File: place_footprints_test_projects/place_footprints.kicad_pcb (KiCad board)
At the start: 2 copper layers, 65 parts

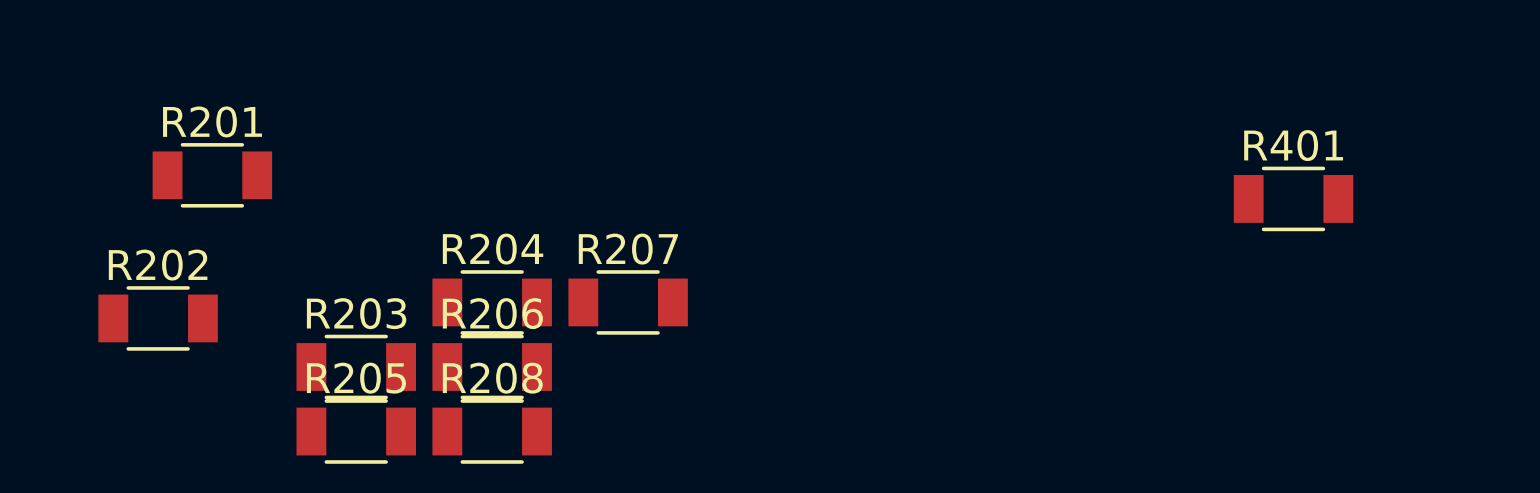
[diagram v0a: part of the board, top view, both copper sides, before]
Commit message: Update make_a_package.sh
Support footprint text placement and rotation

Add support for footprint text placement and rotation
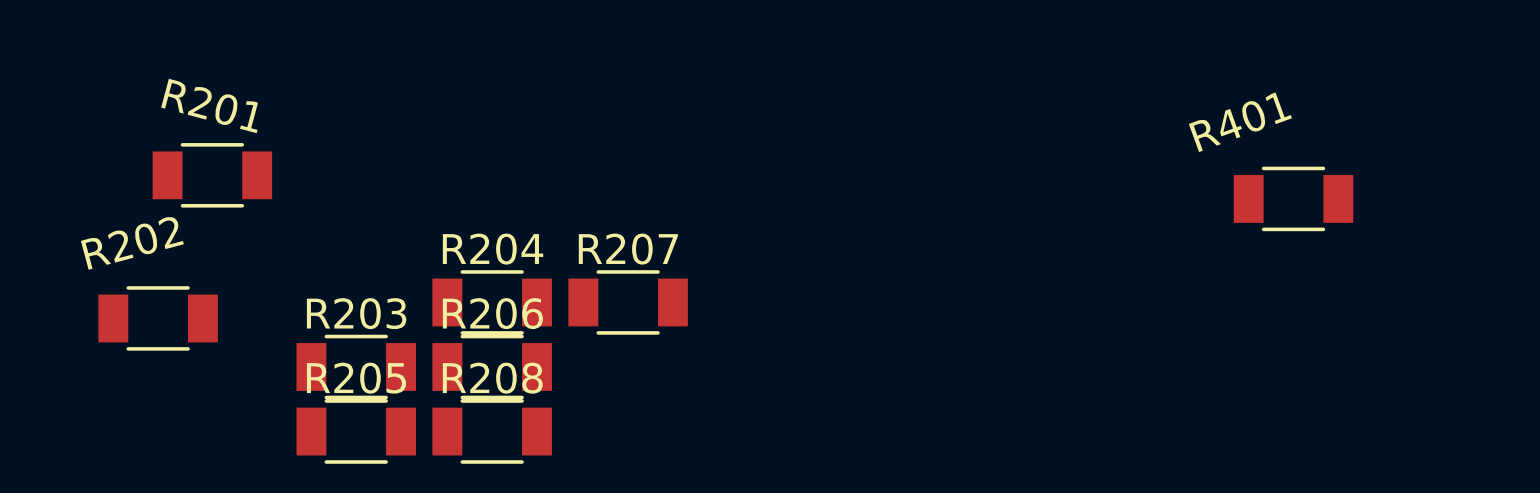
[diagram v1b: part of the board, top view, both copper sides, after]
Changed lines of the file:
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@@
     (property "Sheetname" "Sheet3")
     (attr smd)
-    (fp_text reference "R401" (at 0 -1.75) (layer "F.SilkS")
+    (fp_text reference "R401" (at -1.768 -2.568 20 unlocked) (layer "F.SilkS")
       (effects (font (size 1 1) (thickness 0.15)))
     )
@@
     (property "Sheetname" "Sheet1")
     (attr smd)
-    (fp_text reference "R202" (at 0 -1.75) (layer "F.SilkS")
+    (fp_text reference "R202" (at -0.852 -2.504 15 unlocked) (layer "F.SilkS")
       (effects (font (size 1 1) (thickness 0.15)))
     )
@@
     (property "Sheetname" "Sheet1")
     (attr smd)
-    (fp_text reference "R201" (at 0 -1.75) (layer "F.SilkS")
-      (effects (font (size 1 1) (thickness 0.15)))
-    )
+    (fp_text reference "R201" (at 0 -2.286 -15 unlocked) (layer "F.SilkS")
+      (effects (font (size 1 1) (thickness 0.15)))
+    )

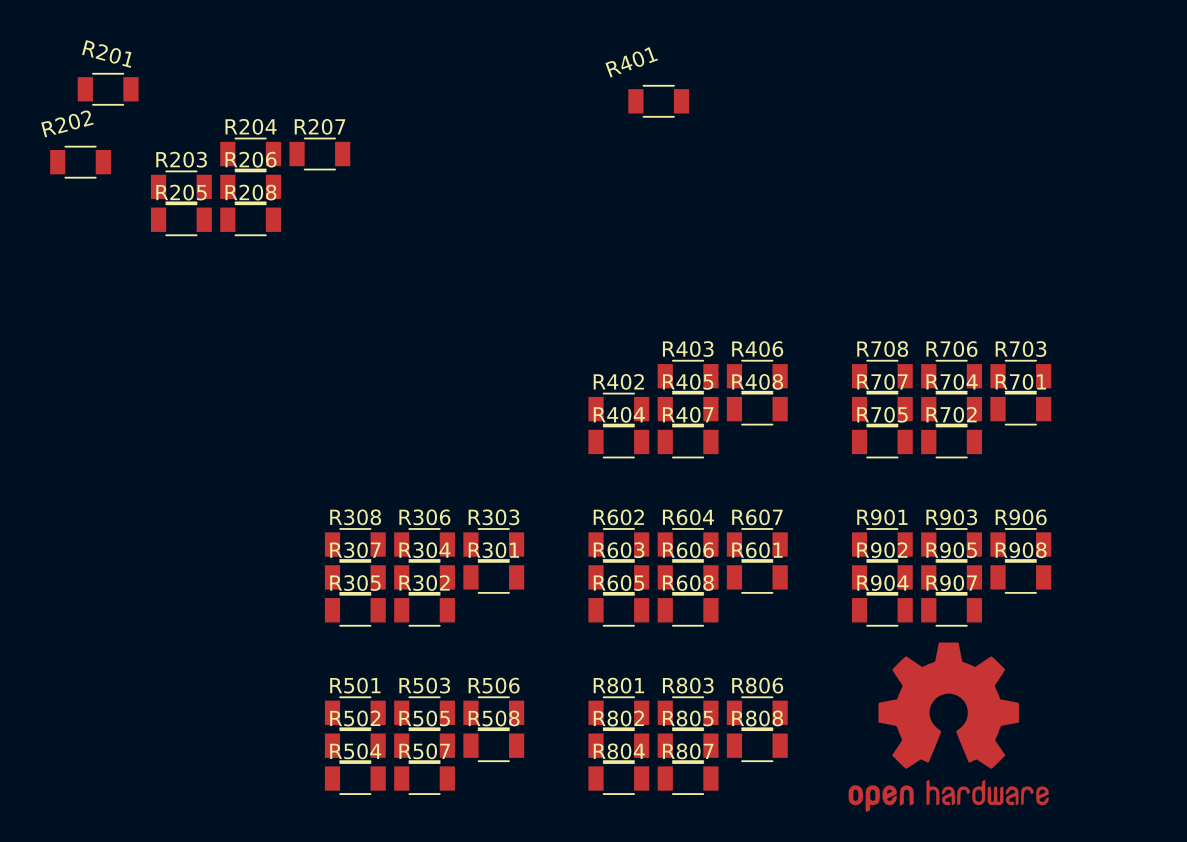
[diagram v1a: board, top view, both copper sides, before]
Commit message: fix placing flipped footprints, update test suite
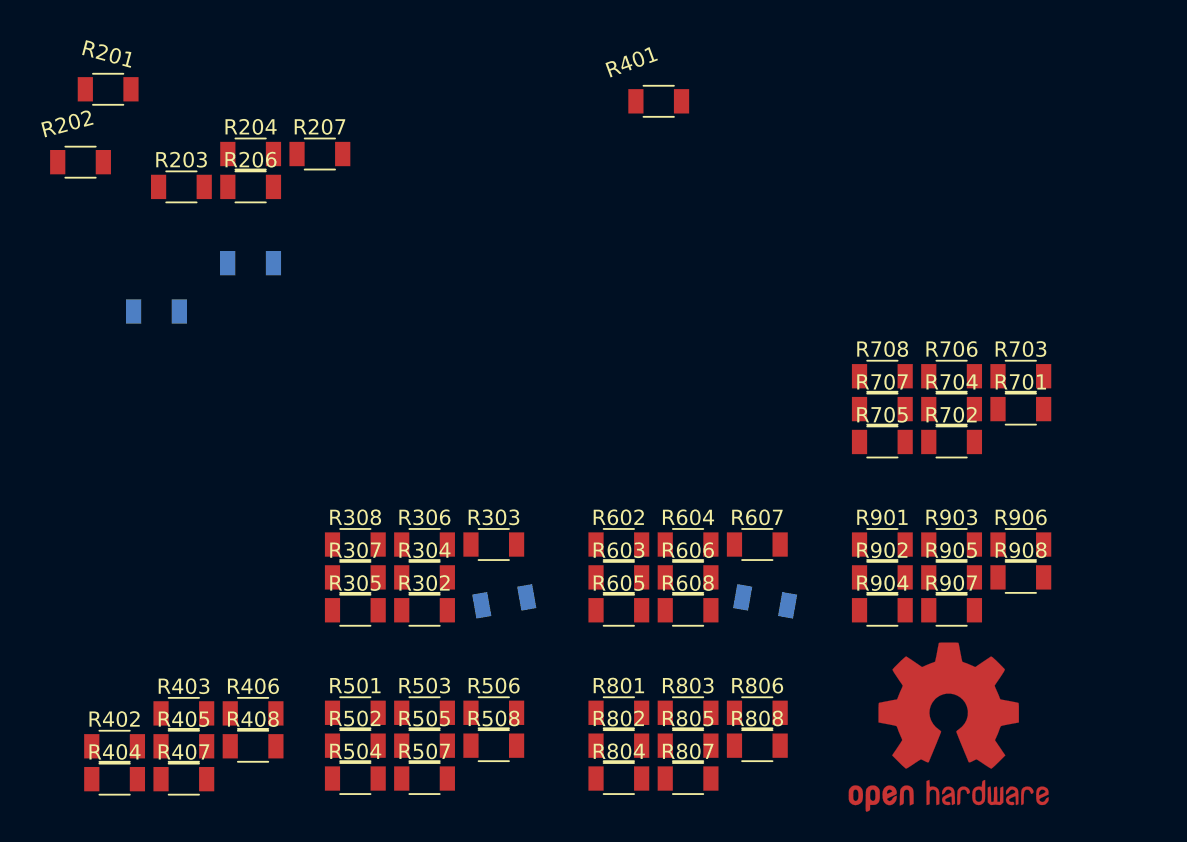
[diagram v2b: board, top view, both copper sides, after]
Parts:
- R205, R208, R301, R601: moved to B.Cu
- moved R403 39.9 mm to (48.8, 70.2)
- moved R405 39.9 mm to (48.8, 72.4)
- moved R406 39.9 mm to (53.3, 70.2)
- moved R407 39.9 mm to (48.8, 74.5)
- moved R402 39.9 mm to (44.2, 72.4)
- moved R404 39.9 mm to (44.2, 74.5)
- moved R408 39.9 mm to (53.3, 72.4)
- moved R205 6.25 mm to (47.0, 43.8), turned to 180 degrees
- moved R208 2.85 mm to (53.2, 40.6), turned to 180 degrees
- moved R301 1.72 mm to (69.8, 62.9), turned to -170 degrees
- moved R601 1.66 mm to (87.0, 62.9), turned to 170 degrees

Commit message: update test project
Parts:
- added R101: R, Resistor_SMD:R_1210_3225Metric_Pad1.30x2.65mm_HandSolder, F.Cu at (110.5, 71.1)
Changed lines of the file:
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@@
   (net 127 "unconnected-(R908-Pad1)")
   (net 128 "unconnected-(R908-Pad2)")
+  (net 129 "unconnected-(R101-Pad1)")
+  (net 130 "unconnected-(R101-Pad2)")
   (footprint "Passives:R1206M" (layer "F.Cu")
     (at 77.380001 70.190001)
@@
       (offset (xyz 0 0 0))
       (scale (xyz 1 1 1))
+      (rotate (xyz 0 0 0))
+    )
+  )
+  (footprint "Resistor_SMD:R_1210_3225Metric_Pad1.30x2.65mm_HandSolder" (layer "F.Cu")
+    (at 110.49 71.12)
+    (descr "Resistor SMD 1210 (3225 Metric), square (rectangular) end terminal, IPC_7351 nominal with elongated pad for handsoldering. (Body size source: IPC-SM-782 page 72, https://www.pcb-3d.com/wordpress/wp-content/uploads/ipc-sm-782a_amendment_1_and_2.pdf), generated with kicad-footprint-generator")
+    (tags "resistor handsolder")
+    (property "Sheetfile" "place_footprints.kicad_sch")
+    (property "Sheetname" "")
+    (attr smd)
+    (fp_text reference "R101" (at 0 -2.28) (layer "F.SilkS")
+      (effects (font (size 1 1) (thickness 0.15)))
+    )
+    (fp_text value "R" (at 0 2.28) (layer "F.Fab")
+      (effects (font (size 1 1) (thickness 0.15)))
+    )
+    (fp_text user "${REFERENCE}" (at 0 0) (layer "F.Fab")
+      (effects (font (size 0.8 0.8) (thickness 0.12)))
+    )
+    (fp_line (start -0.723737 1.355) (end 0.723737 1.355) (layer "F.SilkS") (width 0.12))
+    (fp_line (start -0.723737 -1.355) (end 0.723737 -1.355) (layer "F.SilkS") (width 0.12))
+    (fp_line (start -2.45 -1.58) (end 2.45 -1.58) (layer "F.CrtYd") (width 0.05))
+    (fp_line (start 2.45 -1.58) (end 2.45 1.58) (layer "F.CrtYd") (width 0.05))
+    (fp_line (start -2.45 1.58) (end -2.45 -1.58) (layer "F.CrtYd") (width 0.05))
+    (fp_line (start 2.45 1.58) (end -2.45 1.58) (layer "F.CrtYd") (width 0.05))
+    (fp_line (start 1.6 1.245) (end -1.6 1.245) (layer "F.Fab") (width 0.1))
+    (fp_line (start -1.6 -1.245) (end 1.6 -1.245) (layer "F.Fab") (width 0.1))
+    (fp_line (start 1.6 -1.245) (end 1.6 1.245) (layer "F.Fab") (width 0.1))
+    (fp_line (start -1.6 1.245) (end -1.6 -1.245) (layer "F.Fab") (width 0.1))
+    (pad "1" smd roundrect (at -1.55 0) (size 1.3 2.65) (layers "F.Cu" "F.Paste" "F.Mask") (roundrect_rratio 0.192308)
+      (net 129 "unconnected-(R101-Pad1)") (pintype "passive"))
+    (pad "2" smd roundrect (at 1.55 0) (size 1.3 2.65) (layers "F.Cu" "F.Paste" "F.Mask") (roundrect_rratio 0.192308)
+      (net 130 "unconnected-(R101-Pad2)") (pintype "passive"))
+    (model "${KICAD6_3DMODEL_DIR}/Resistor_SMD.3dshapes/R_1210_3225Metric.wrl"
+      (offset (xyz 0 0 0))
+      (scale (xyz 1 1 1))
